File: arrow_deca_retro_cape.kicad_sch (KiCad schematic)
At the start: 80 parts, among them J1 DB15_Female_HighDensity_Mount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, J10 Conn_02x06_Odd_Even, J11 PMOD1, J12 PMOD2, J14 Conn_01x02, J15 Conn_01x03, J16 Conn_01x06, J17 Conn_01x02, J18 Conn_01x03, J19 DINC_MIN_TM_6_1, J2 Conn_02x01, J20 PMOD3, J21 USB3_A, J22 Conn_01x03, J3 Conn_02x01, J4 DB9_Male_MountingHoles, J5 DINC_MIN_TM_6_1, J6 Conn_02x20_Odd_Even, J7 Conn_01x03, J8 P8_Male, J9 P9_Male, U4 LM1117-3.3, U5 LM1117-2.5

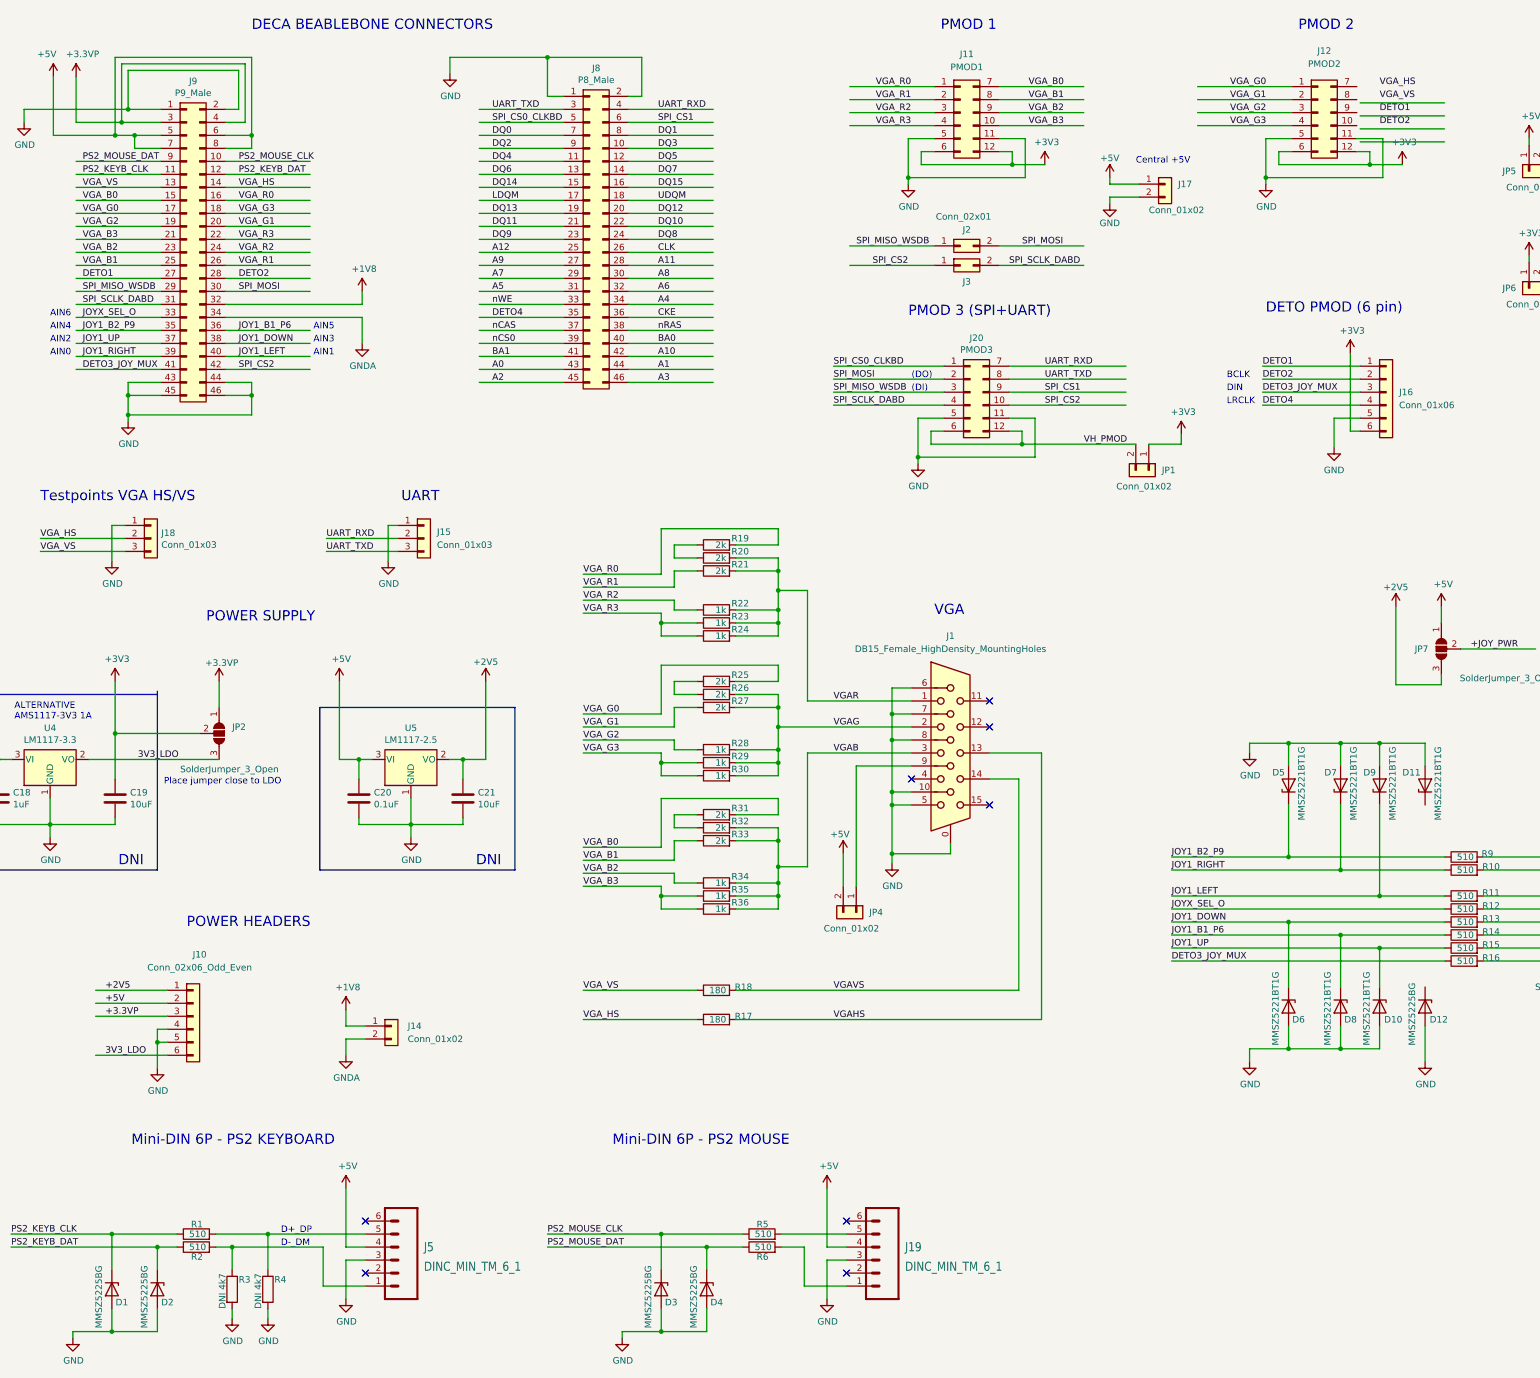
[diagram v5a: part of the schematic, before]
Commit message: v0.78 ps2 protections with zeners
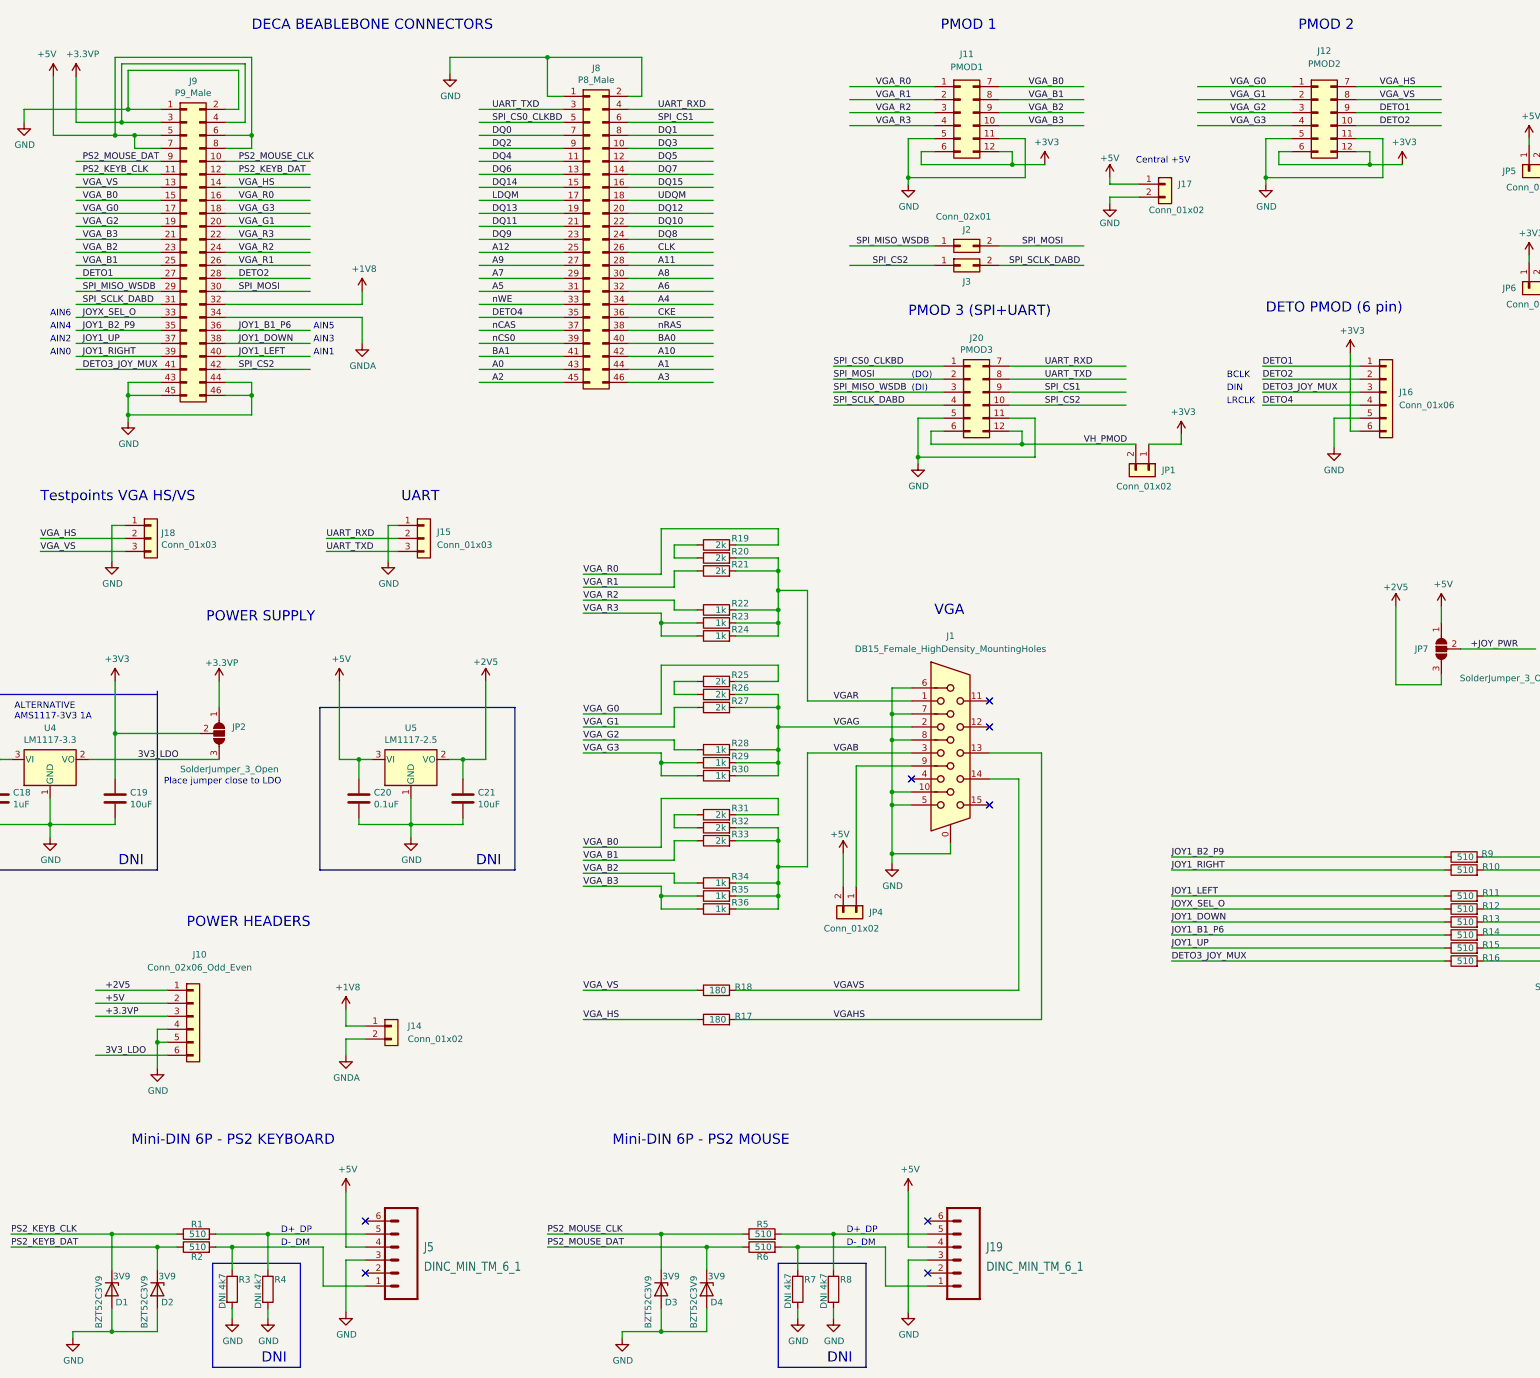
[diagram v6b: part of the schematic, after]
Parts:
- removed D10, D11, D5, D6, D7, D8, D9: MMSZ5221BT1G, Diode_SMD:D_SOD-123, symbol Diode:BZT52Bxx
- removed D12: MMSZ5225BG, Diode_SMD:D_SOD-123, symbol Diode:BZT52Bxx
- added R7, R8: DNI 4k7, Resistor_SMD:R_0805_2012Metric_Pad1.20x1.40mm_HandSolder, symbol Device:R
- D1, D2, D3, D4: value MMSZ5225BG -> BZT52C3V9; Vz (none) -> 3V9
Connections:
- net DETO1: now also J12.9 (Pin_9)
- net DETO2: now also J12.10 (Pin_10)
- net GND: now also R7.2, R8.2
- net VGA_HS: now also J12.7 (Pin_7)
- net VGA_VS: now also J12.8 (Pin_8)
- net at J19.1, R6.2: now also R7.1
- net at J19.5, R5.2: now also R8.1
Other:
- moved on the sheet: J19

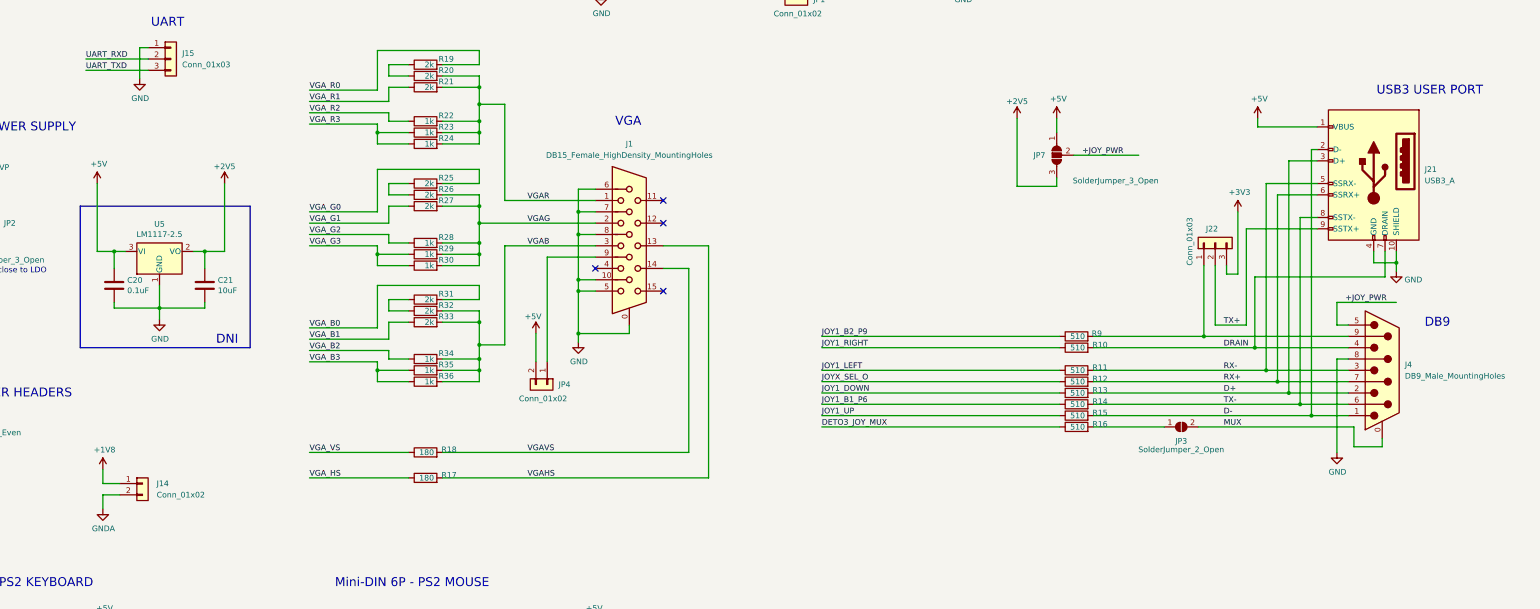
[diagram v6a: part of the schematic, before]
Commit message: v0.80 WIP adding level shifter for db9/usb3
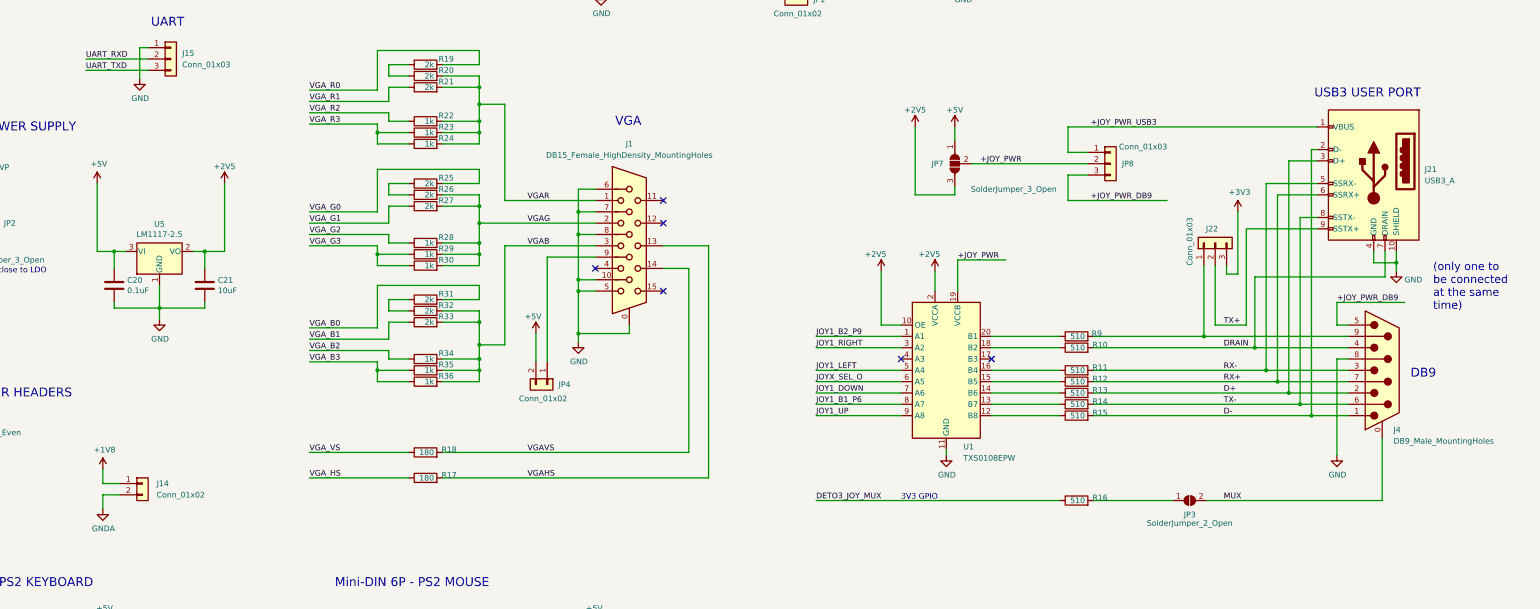
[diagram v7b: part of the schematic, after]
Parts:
- added JP8: Conn_01x03, Connector_PinHeader_2.54mm:PinHeader_1x03_P2.54mm_Vertical, symbol Connector_Generic:Conn_01x03
- added U1: TXS0108EPW, Package_SO:TSSOP-20_4.4x6.5mm_P0.65mm, symbol Logic_LevelTranslator:TXS0108EPW
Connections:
- net +2V5: now also U1.10 (OE), U1.2 (VCCA)
- net +5V: no longer J21.1 (VBUS)
- net +JOY_PWR: now also JP8.2 (Pin_2), U1.19 (VCCB); no longer J4.5
- net GND: now also U1.11 (GND)
- net JOY1_B1_P6: now also U1.8 (A7); no longer R14.1
- net JOY1_B2_P9: now also U1.1 (A1); no longer R9.1
- net JOY1_DOWN: now also U1.7 (A6); no longer R13.1
- net JOY1_LEFT: now also U1.5 (A4); no longer R11.1
- net JOY1_RIGHT: now also U1.3 (A2); no longer R10.1
- net JOY1_UP: now also U1.9 (A8); no longer R15.1
- net JOYX_SEL_O: now also U1.6 (A5); no longer R12.1
- new net: R15.1, U1.12 (B8)
- new net: R11.1, U1.16 (B4)
- new net: R13.1, U1.14 (B6)
- new net: R9.1, U1.20 (B1)
- new net: R14.1, U1.13 (B7)
- new net: R12.1, U1.15 (B5)
- new net: R10.1, U1.18 (B2)
- new net +JOY_PWR_DB9: J4.5, JP8.3 (Pin_3)
- new net +JOY_PWR_USB3: J21.1 (VBUS), JP8.1 (Pin_1)
- no-connect marks 8 -> 10
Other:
- note added: "(only one to be connected at the same time)"
- note added: "3V3 GPIO"
- moved on the sheet: JP3, JP7, R16

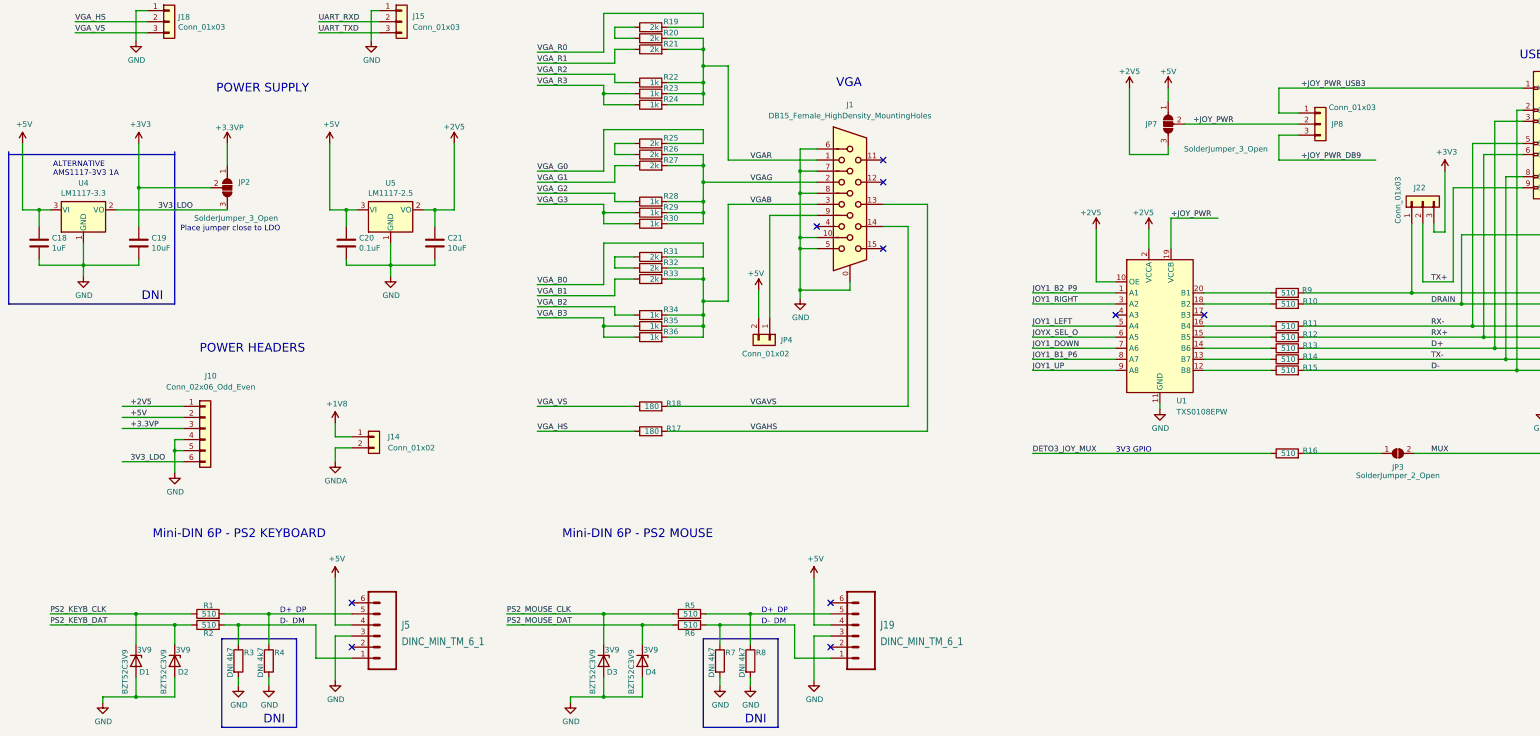
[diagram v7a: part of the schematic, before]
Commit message: v0.8 routing ended for level shifter
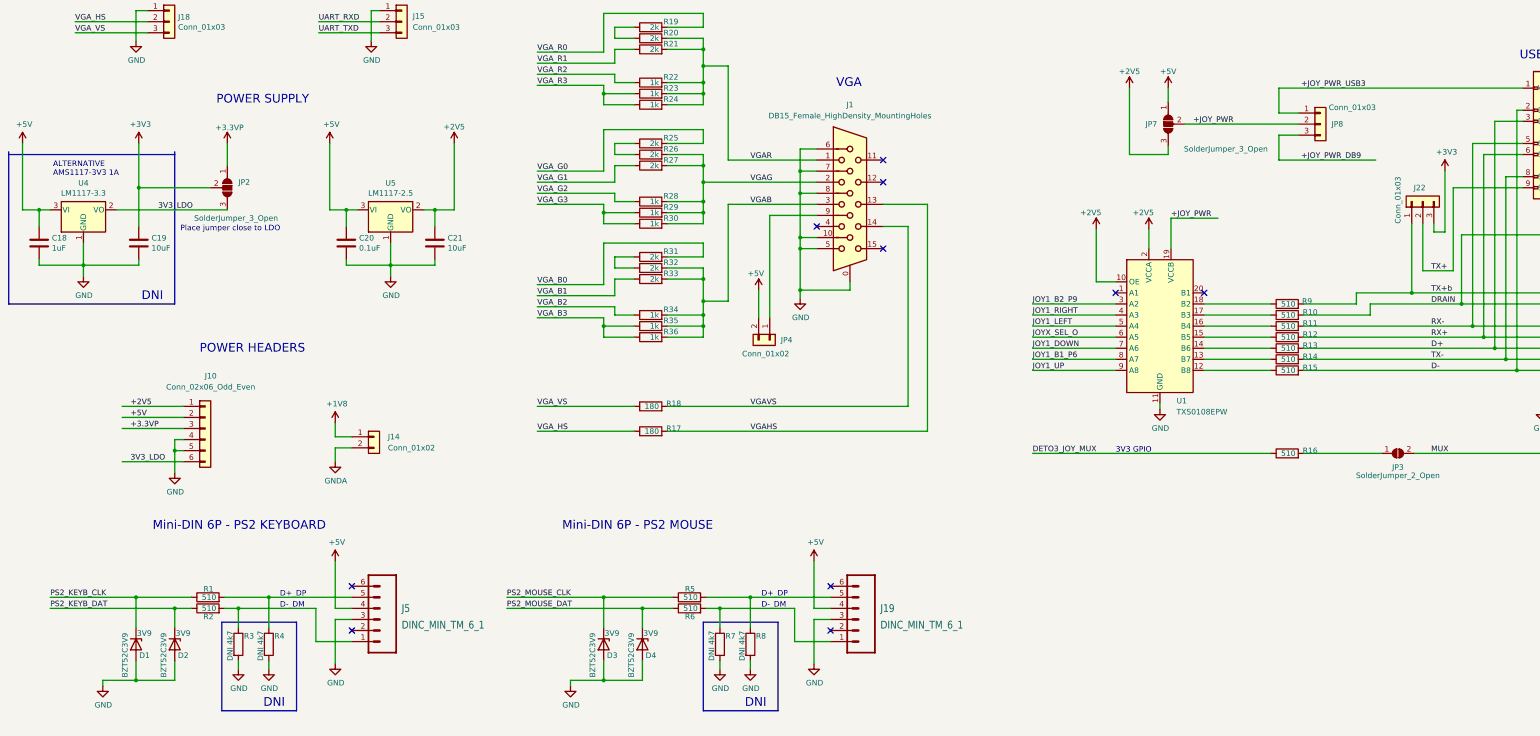
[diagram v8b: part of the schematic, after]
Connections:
- net JOY1_B2_P9: now also U1.3 (A2); no longer U1.1 (A1)
- net JOY1_RIGHT: now also U1.4 (A3); no longer U1.3 (A2)
- net at R9.1: now also U1.18 (B2); no longer U1.20 (B1)
- net TX+b: now reaches J22.1 (Pin_1), J4.9, R9.2
- net at U1.17 (B3): now also R10.1
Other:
- moved on the sheet: D1, D2, D3, D4, J19, J5, R1, R10, R2, R3, R4, R5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
